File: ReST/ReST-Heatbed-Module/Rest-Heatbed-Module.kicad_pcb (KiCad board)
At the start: 2 copper layers, 16 parts, among them P1 02-SCREW-TERM, P2 02X04-MALE, P3 02-SCREW-TERM, P4 01X02-MALE, P5 02-SCREW-TERM, Q1 Q_BSH105, Q2 Q_AOT240L

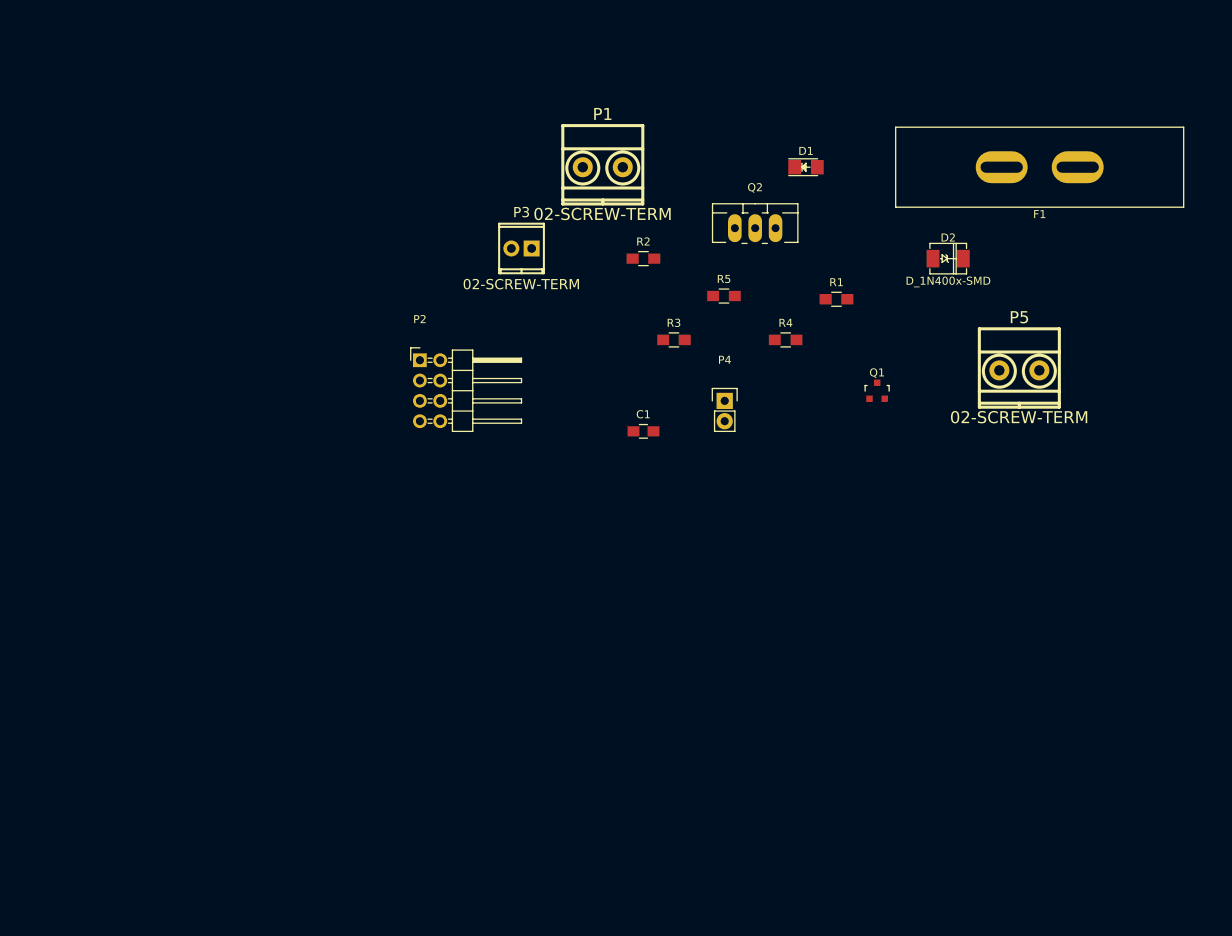
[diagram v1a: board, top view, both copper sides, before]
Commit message: Layout for Heatbed PCB
Basic layout for the heatbed pcb is finished. single sided load, so its easier for reflow. need to work on the traces now. size shouldnt change by now.
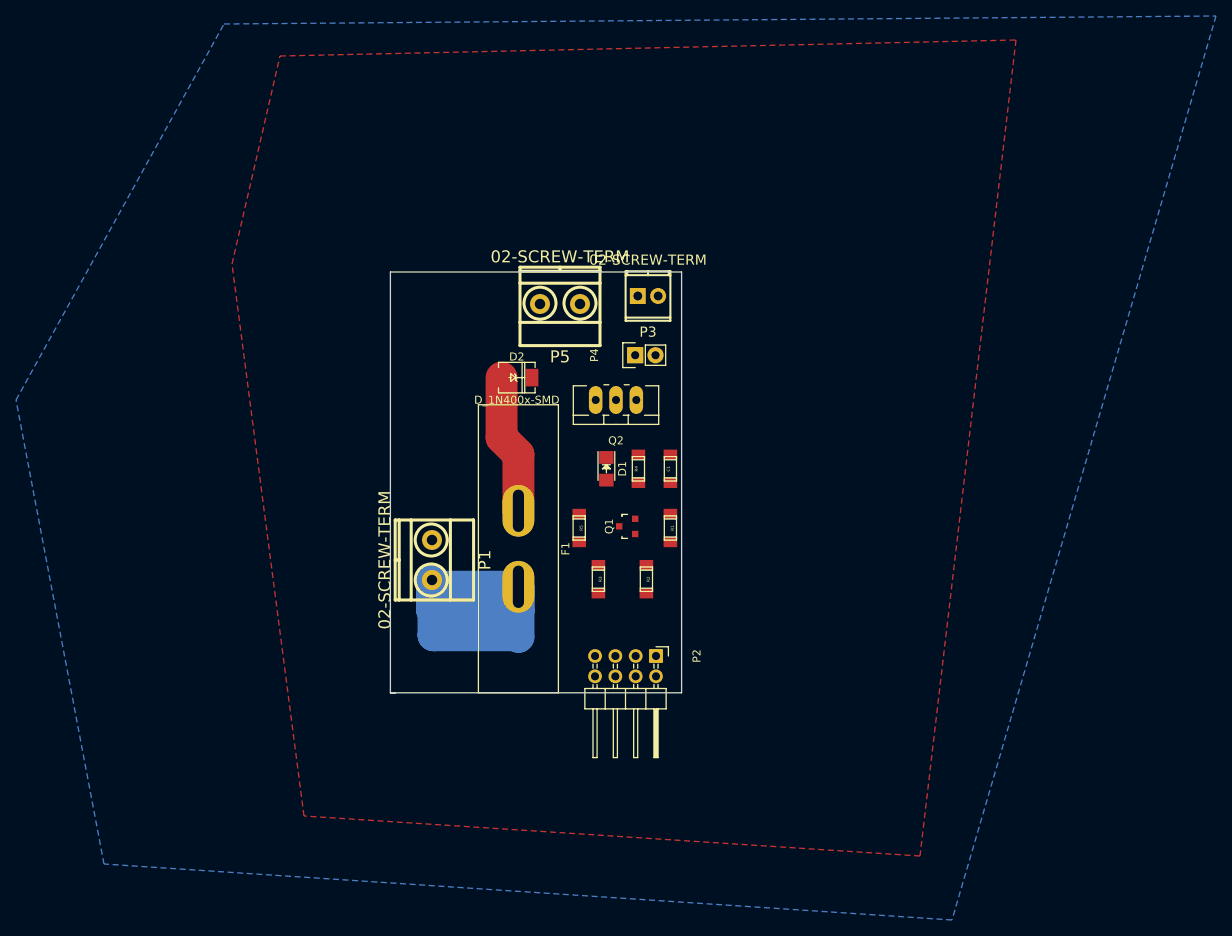
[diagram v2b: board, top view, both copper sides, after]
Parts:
- C1: footprint Capacitors_SMD:C_0805_HandSoldering -> ok-smd-generic:1206
- R1, R2, R3, R4, R5: footprint Resistors_SMD:R_0805_HandSoldering -> ok-smd-generic:1206
- moved F1 80.8 mm to (122.8, 136.6), turned to 90 degrees
- moved P5 58.0 mm to (128.0, 106.0), turned to 180 degrees
- moved D2 55.9 mm to (122.6, 115.2)
- moved P1 53.5 mm to (112.0, 138.0), turned to 270 degrees
- moved P2 47.3 mm to (140.0, 150.0), turned to 270 degrees
- moved D1 45.2 mm to (133.8, 126.6), turned to 270 degrees
- moved R2 40.1 mm to (138.8, 140.4), turned to 270 degrees
- moved Q1 35.5 mm to (136.4, 133.8), turned to 90 degrees
- moved R1 35.3 mm to (141.8, 134.0), turned to 270 degrees
- moved R5 34.2 mm to (130.4, 134.0), turned to 270 degrees
- moved R3 31.4 mm to (132.8, 140.4), turned to 270 degrees
- moved Q2 27.6 mm to (135.0, 118.0), turned to 180 degrees
- moved R4 24.5 mm to (137.8, 126.6), turned to 90 degrees
- moved P3 16.9 mm to (139.0, 105.0), turned to 180 degrees
- moved P4 12.6 mm to (137.4, 112.4), turned to 90 degrees
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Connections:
- P5 pad 1: +12V -> Net-(D2-Pad2)
- P5 pad 2: Net-(D2-Pad2) -> +12V
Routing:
- net Net-(F1-Pad1): track 0.00 -> 52.9 mm
- net +12V: track 0.00 -> 17.5 mm
- added copper zone on B.Cu, net GND
- added copper zone on F.Cu, net GND
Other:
- board outline added: 36.4 x 52.6 mm
